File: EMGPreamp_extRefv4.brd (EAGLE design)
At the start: 28.4 x 31.6 mm, 33 parts

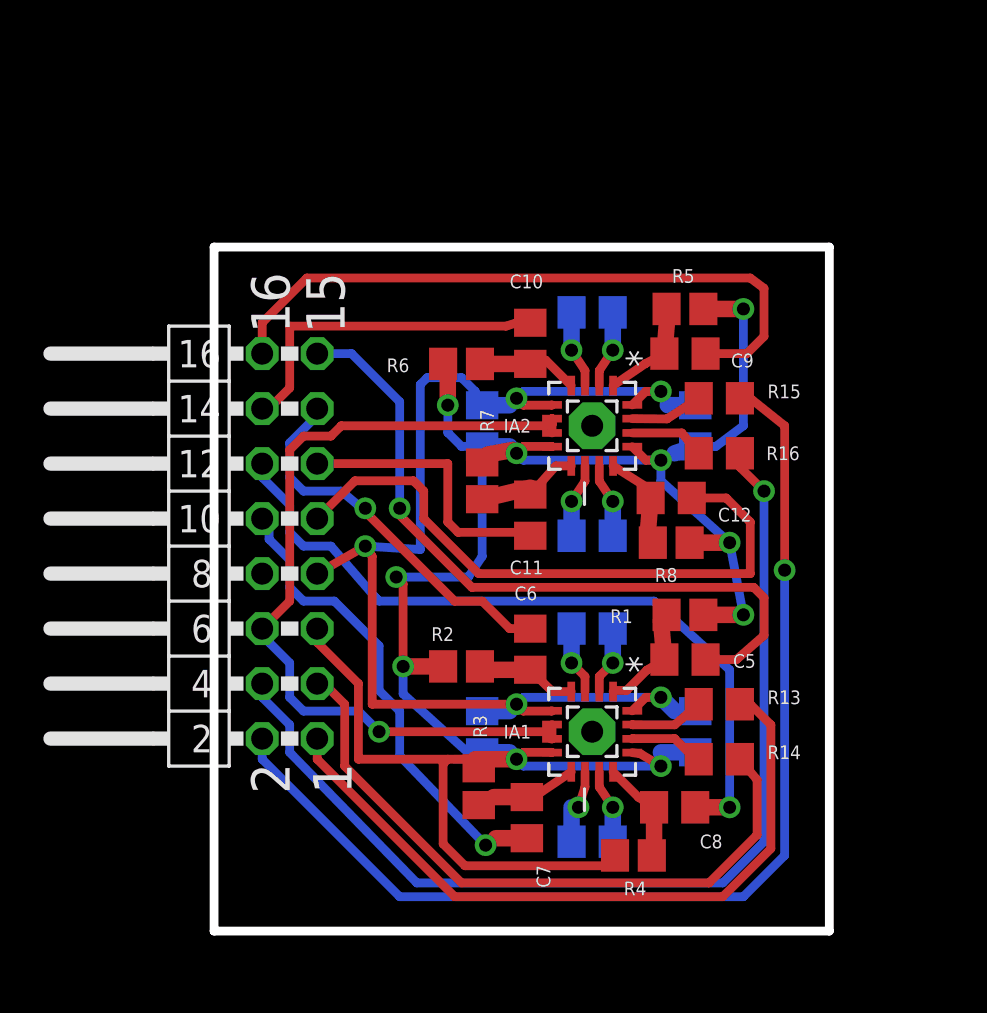
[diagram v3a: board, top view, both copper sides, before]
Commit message: updated design to add RF lowpass and decoupling to input. Also added real ground plane and VREF plane to help isolate inputs from noise
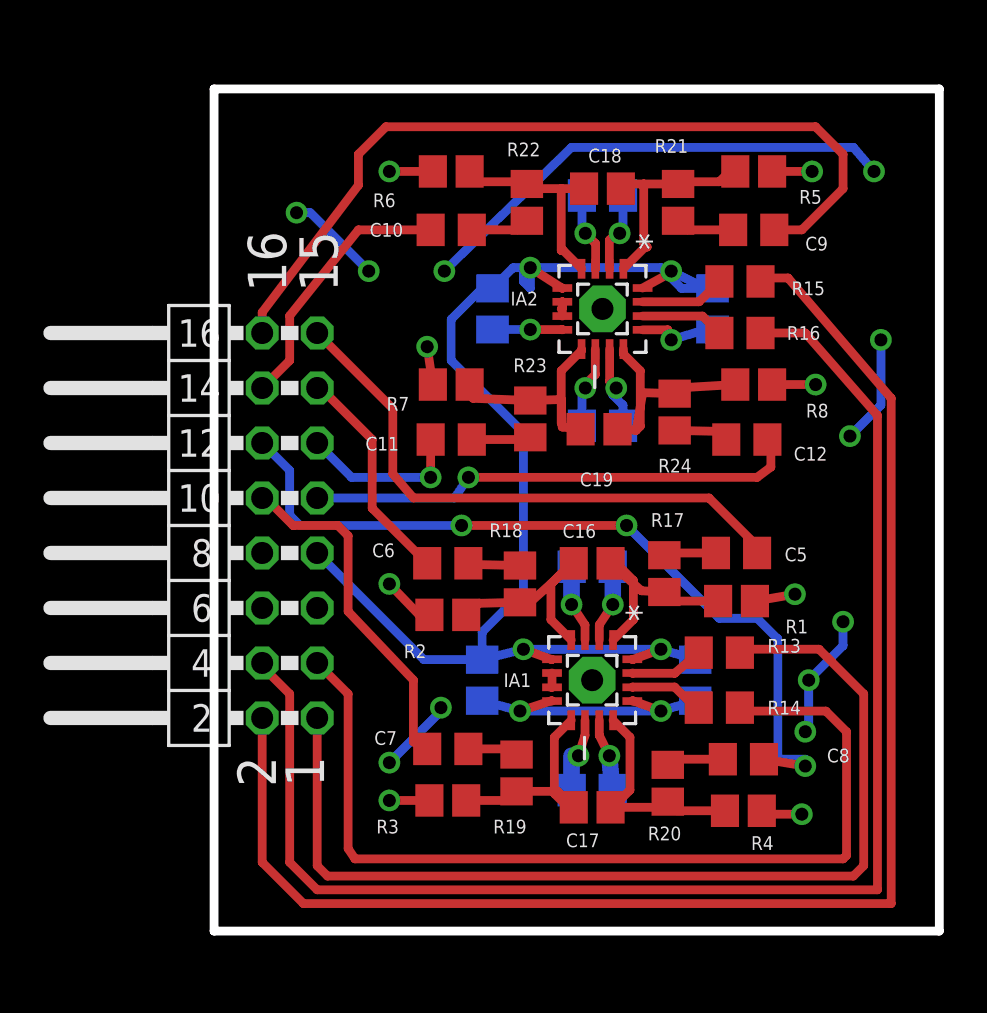
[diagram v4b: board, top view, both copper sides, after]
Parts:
- added C16, C17, C18, C19: 100p, resistor:C0805
- added R17, R18, R19, R20, R21, R22, R23, R24: 10k, resistor:R0805
- moved R6 8.90 mm to (10.0, 34.1)
- moved R8 8.24 mm to (24.0, 24.3)
- moved R5 7.10 mm to (24.0, 34.1)
- moved C9 6.54 mm to (24.0, 31.4)
- moved C10 6.39 mm to (10.0, 31.4), turned to 0 degrees
- moved R16 5.64 mm to (23.3, 26.7)
- moved C6 5.50 mm to (9.84, 16.0), turned to 0 degrees
- moved R4 5.48 mm to (23.5, 4.60), turned to 180 degrees
- moved R15 5.48 mm to (23.3, 29.1)
- moved C5 5.47 mm to (23.2, 16.5)
- moved C4 5.46 mm to (22.1, 27.8)
- moved R11 5.42 mm to (17.0, 33.0)
- moved C3 5.42 mm to (11.9, 27.8)
- moved IA2 5.42 mm to (17.0, 27.8)
- moved PAD1 5.42 mm to (17.0, 27.8)
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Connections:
- new net N$1: C5.2, R17.1
- new net N$2: C6.2, R18.1
- new net N$3: C8.2, R20.1
- new net N$4: C9.2, R21.1
- new net N$5: C10.2, R22.1
- new net N$6: C7.2, R19.1
- new net N$7: C11.2, R23.1
- new net N$8: C12.2, R24.1
- net I11: now also C16.1, R17.2; no longer C5.2
- net I12: now also C16.2, R18.2; no longer C6.2
- net I13: now also C17.1, R19.2; no longer C7.2
- net I14: now also C17.2, R20.2; no longer C8.2
- net I21: now also C18.1, R21.2; no longer C9.2
- net I22: now also C18.2, R22.2; no longer C10.2
- net I23: now also C19.1, R23.2; no longer C11.2
- net I24: now also C19.2, R24.2; no longer C12.2
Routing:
- net GND: track 107.2 -> 36.0 mm, vias 10 -> 12
- net OUT4: track 47.3 -> 66.4 mm, vias 1 -> 0
- net OUT3: track 50.9 -> 68.5 mm, vias 1 -> 0
- net OUT1: track 33.0 -> 47.0 mm
- net OUT2: track 30.5 -> 43.6 mm
- net IN1+: track 18.4 -> 10.3 mm, vias 1 -> 0
- net IN3-: track 30.9 -> 38.7 mm
- net I24: track 4.60 -> 11.2 mm
- net IN1-: track 33.2 -> 26.7 mm, vias 1 -> 0
- net IN4+: track 14.1 -> 7.64 mm, vias 0 -> 1
- net IN4-: track 29.1 -> 23.0 mm, vias 0 -> 1
- net I12: track 4.66 -> 10.4 mm
- net I23: track 5.09 -> 10.7 mm
- net I14: track 4.75 -> 10.3 mm
- net I22: track 4.73 -> 10.1 mm
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- added copper zone on layer 16, net GND
- added copper zone on layer 16, net N$9
- added copper zone on layer 1, net VREF
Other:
- board size 28.4 x 31.6 mm -> 33.5 x 38.9 mm
- board text added: "Aug 2017"
- board text added: "V4 rev2"
- board text removed: "Aug 2016"
- board text removed: "V4 rev1"

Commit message: minor routing changes to increase VREF plane coverage
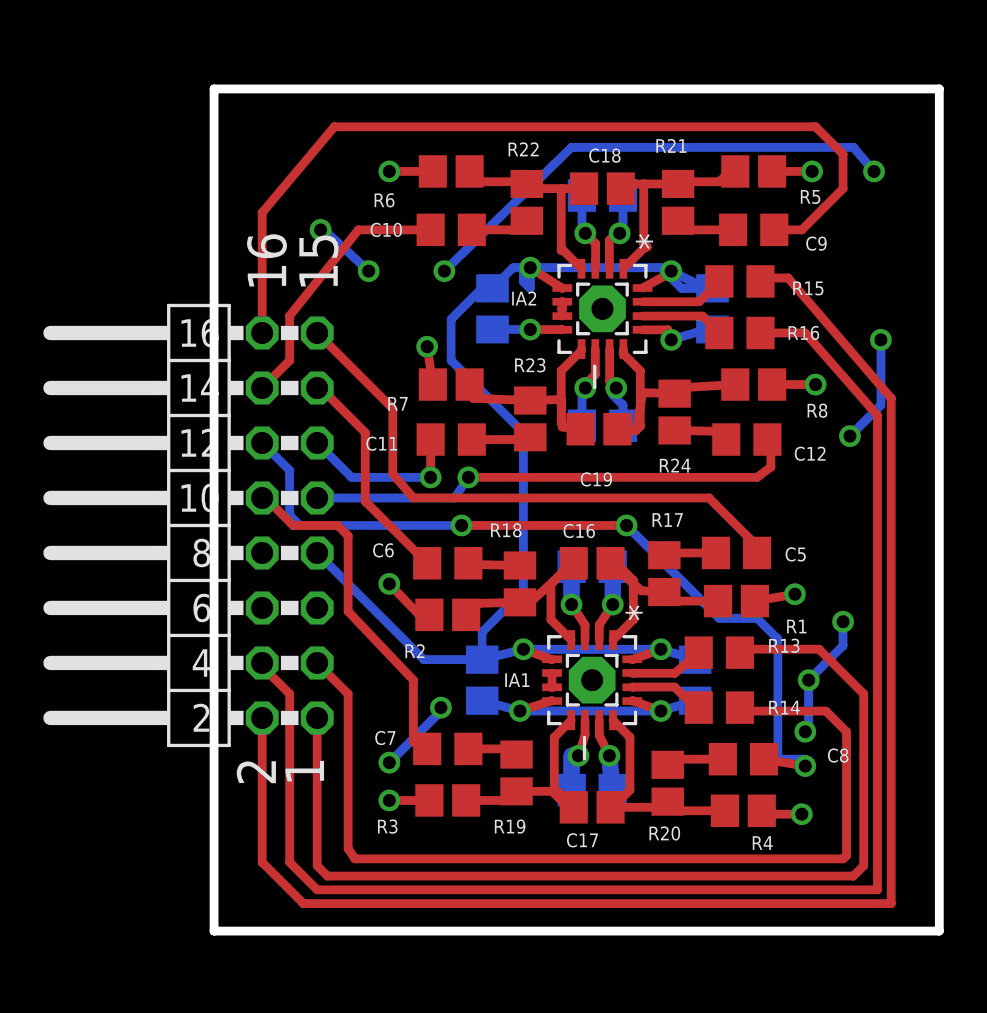
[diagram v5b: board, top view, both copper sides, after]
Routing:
- net IN3-: track 38.7 -> 40.3 mm
- net VREF: track 43.2 -> 41.8 mm
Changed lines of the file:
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@@
 <wire x1="7.14375" y1="6.82625" x2="9.525" y2="9.2075" width="0.4064" layer="16"/>
 <wire x1="9.525" y1="9.2075" x2="9.525" y2="9.36625" width="0.4064" layer="16"/>
-<via x="2.8575" y="32.22625" extent="1-16" drill="0.6" shape="square"/>
+<via x="3.96875" y="31.4325" extent="1-16" drill="0.6" shape="square"/>
 <via x="6.19125" y="29.5275" extent="1-16" drill="0.6" shape="square"/>
 <via x="28.41625" y="21.9075" extent="1-16" drill="0.6" shape="square"/>
 <via x="29.845" y="26.3525" extent="1-16" drill="0.6" shape="square"/>
-<wire x1="6.19125" y1="29.5275" x2="3.4925" y2="32.22625" width="0.4064" layer="16"/>
-<wire x1="3.4925" y1="32.22625" x2="2.8575" y2="32.22625" width="0.4064" layer="16"/>
+<wire x1="6.19125" y1="29.5275" x2="4.1275" y2="31.4325" width="0.4064" layer="16"/>
+<wire x1="4.1275" y1="31.4325" x2="3.96875" y2="31.4325" width="0.4064" layer="16"/>
 <wire x1="28.41625" y1="21.9075" x2="29.845" y2="23.33625" width="0.4064" layer="16"/>
 <wire x1="29.845" y1="23.33625" x2="29.845" y2="26.3525" width="0.4064" layer="16"/>
@@
 <contactref element="C6" pad="1"/>
 <contactref element="SV1" pad="13"/>
-<wire x1="6.35" y1="18.57375" x2="8.8925" y2="16.03375" width="0.4064" layer="1"/>
-<wire x1="6.35" y1="18.57375" x2="6.35" y2="21.74875" width="0.4064" layer="1"/>
-<wire x1="6.35" y1="21.74875" x2="3.96875" y2="24.13" width="0.4064" layer="1"/>
+<wire x1="6.0325" y1="18.89125" x2="8.8925" y2="16.03375" width="0.4064" layer="1"/>
+<wire x1="6.0325" y1="18.89125" x2="6.0325" y2="22.06625" width="0.4064" layer="1"/>
+<wire x1="6.0325" y1="22.06625" x2="3.96875" y2="24.13" width="0.4064" layer="1"/>
 <wire x1="3.96875" y1="24.13" x2="3.81" y2="24.13" width="0.4064" layer="1"/>
 </signal>
@@
 <contactref element="C9" pad="1"/>
 <contactref element="SV1" pad="16"/>
-<wire x1="1.27" y1="26.67" x2="1.27" y2="27.6225" width="0.4064" layer="1"/>
-<wire x1="1.27" y1="27.6225" x2="5.715" y2="33.49625" width="0.4064" layer="1"/>
-<wire x1="5.715" y1="33.49625" x2="5.715" y2="34.925" width="0.4064" layer="1"/>
-<wire x1="5.715" y1="34.925" x2="6.985" y2="36.195" width="0.4064" layer="1"/>
-<wire x1="6.985" y1="36.195" x2="26.82875" y2="36.195" width="0.4064" layer="1"/>
+<wire x1="1.27" y1="26.67" x2="1.27" y2="32.22625" width="0.4064" layer="1"/>
+<wire x1="1.27" y1="32.22625" x2="4.60375" y2="36.195" width="0.4064" layer="1"/>
+<wire x1="4.60375" y1="36.195" x2="26.82875" y2="36.195" width="0.4064" layer="1"/>
 <wire x1="26.82875" y1="36.195" x2="28.09875" y2="34.925" width="0.4064" layer="1"/>
 <wire x1="28.09875" y1="34.925" x2="28.09875" y2="33.3375" width="0.4064" layer="1"/>

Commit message: updated RF input suppression to include decoupling caps to gnd
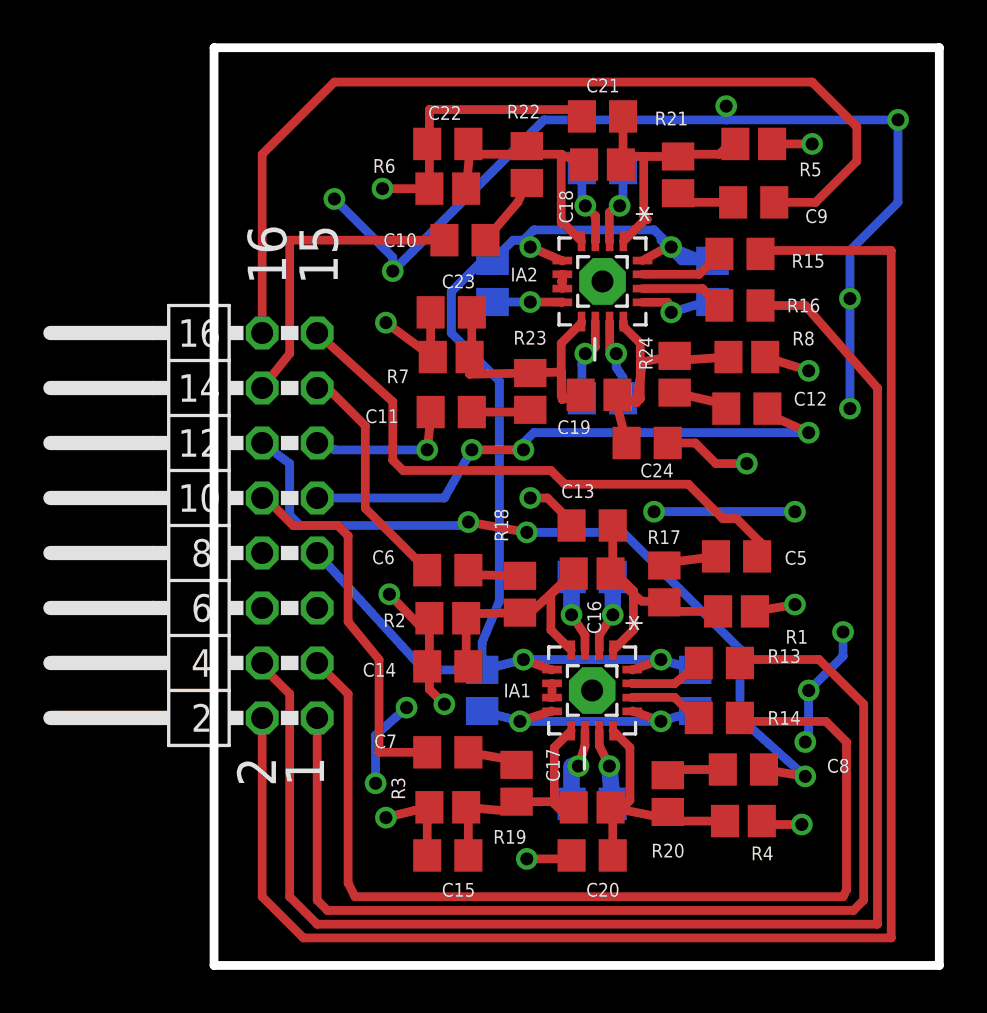
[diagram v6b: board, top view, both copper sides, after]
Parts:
- added C13, C14, C15, C20, C21, C22, C23, C24: 0.1uF, rcl:C0805
- C16, C17, C18, C19: value 100p -> 10uF
- moved R24 1.75 mm to (20.3, 24.8)
- moved R22 1.75 mm to (13.5, 34.4)
- moved C19 1.59 mm to (16.8, 23.8)
- moved C12 1.43 mm to (23.7, 23.2)
- moved R8 1.31 mm to (23.7, 25.6)
- moved C11 1.27 mm to (10.0, 23.0)
- moved C3 1.27 mm to (11.9, 29.1)
- moved C4 1.27 mm to (22.1, 29.1)
- moved C9 1.27 mm to (24.0, 32.7)
- moved IA2 1.27 mm to (17.0, 29.1)
- moved PAD1 1.27 mm to (17.0, 29.1)
- moved R12 1.27 mm to (17.0, 23.7)
- moved R15 1.27 mm to (23.3, 30.3)
- moved R16 1.27 mm to (23.3, 27.9)
- moved R23 1.27 mm to (13.7, 24.0)
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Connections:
- net GND: now also C13.2, C14.2, C15.2, C20.2, C21.2, C22.2, C23.2, C24.2
- net I11: now also C13.1
- net I12: now also C14.1
- net I13: now also C15.1
- net I14: now also C20.1
- net I21: now also C21.1
- net I22: now also C22.1
- net I23: now also C23.1
- net I24: now also C24.1
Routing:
- net GND: track 36.0 -> 66.7 mm, vias 12 -> 16
- net VREF: track 41.8 -> 63.8 mm, vias 11 -> 13
- net OUT3: track 68.5 -> 75.9 mm
- net OUT4: track 66.4 -> 70.9 mm
- net IN4-: track 23.0 -> 26.9 mm, vias 1 -> 3
- net IN3-: track 40.3 -> 44.1 mm
- net OUT2: track 43.6 -> 46.6 mm
- net I12: track 10.4 -> 13.1 mm
- net OUT1: track 47.0 -> 49.7 mm
- net I23: track 10.7 -> 13.2 mm
- net I22: track 10.1 -> 12.6 mm
- net I21: track 10.1 -> 12.5 mm
- net I13: track 10.3 -> 12.5 mm
- net I24: track 11.2 -> 13.4 mm
- net I14: track 10.3 -> 12.5 mm
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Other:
- board size 33.5 x 38.9 mm -> 33.5 x 42.4 mm
